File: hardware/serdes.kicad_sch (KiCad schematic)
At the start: 21 parts, among them U4 GateMate-CCGM1A1, X2 511FCA100M000BAG

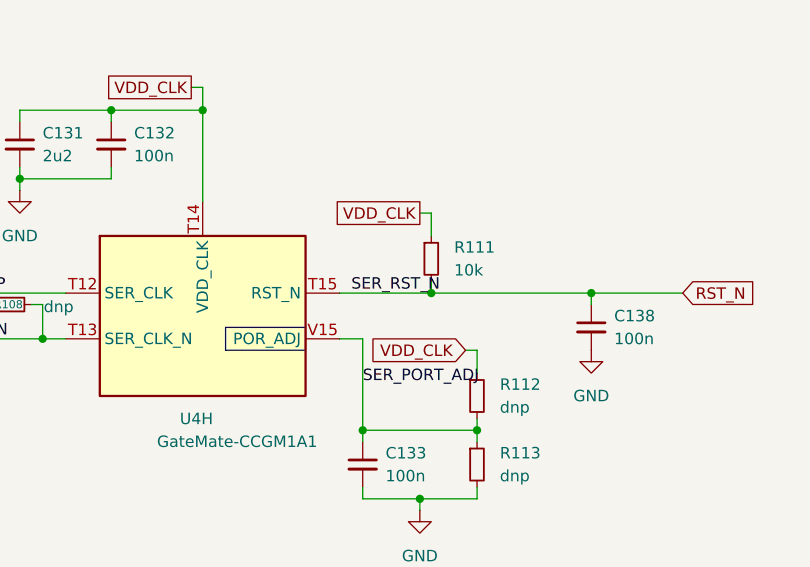
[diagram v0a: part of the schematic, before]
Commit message: power: removed rc filters from gpio domains
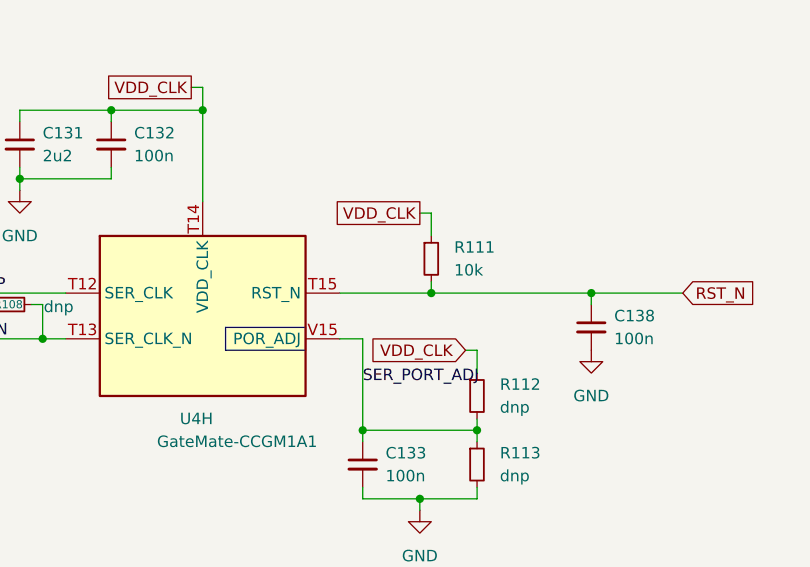
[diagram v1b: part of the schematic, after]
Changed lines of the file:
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@@
-		)
-	)
-	(label "SER_RST_N"
-		(at 125.73 86.36 0)
-		(effects
-			(font
-				(size 1.27 1.27)
-			)
-			(justify left bottom)
 		)
 	)

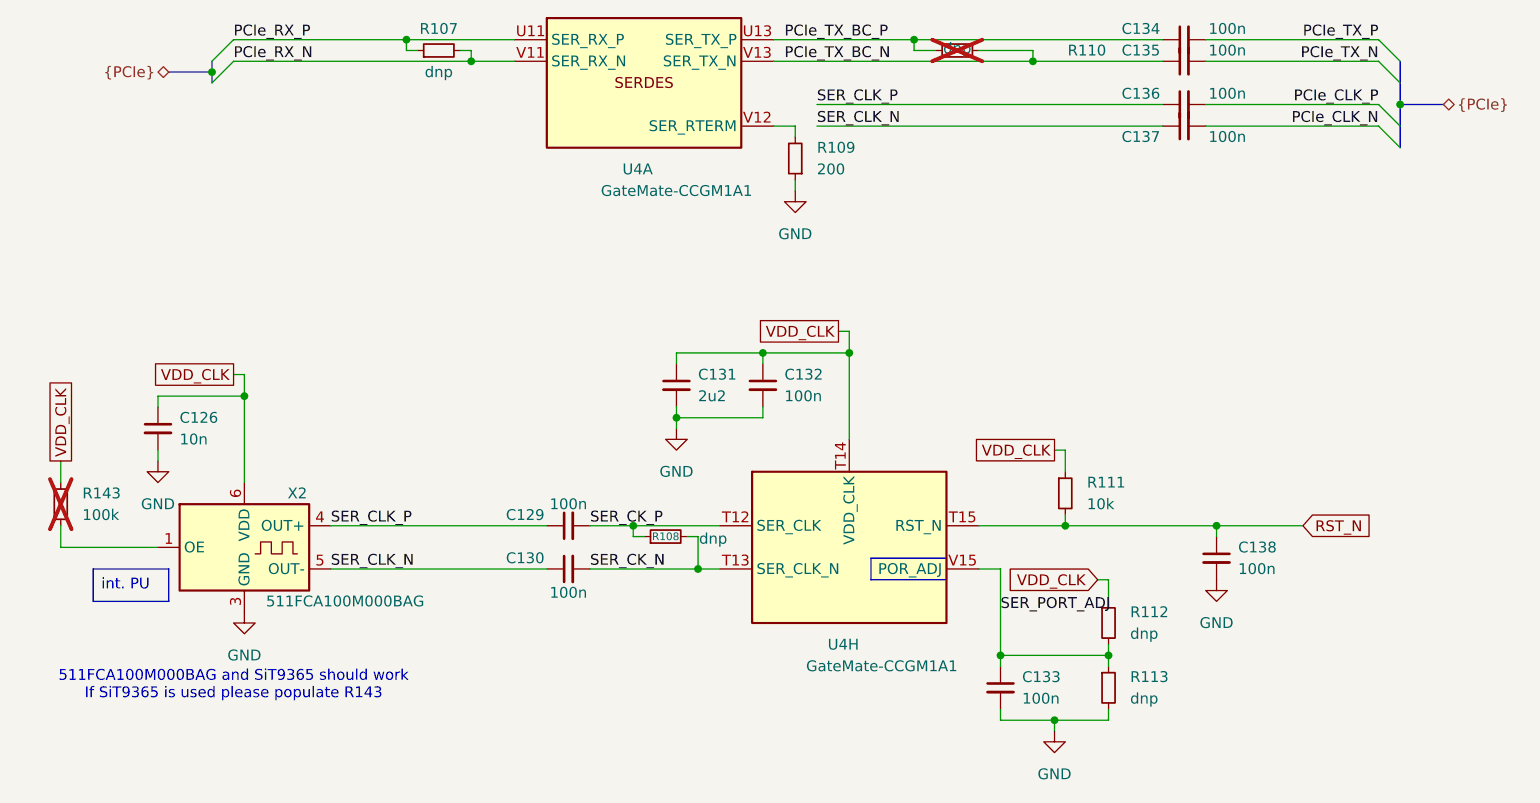
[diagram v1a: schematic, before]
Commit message: serdes: use +1V8 instead of `VDD_CLK`
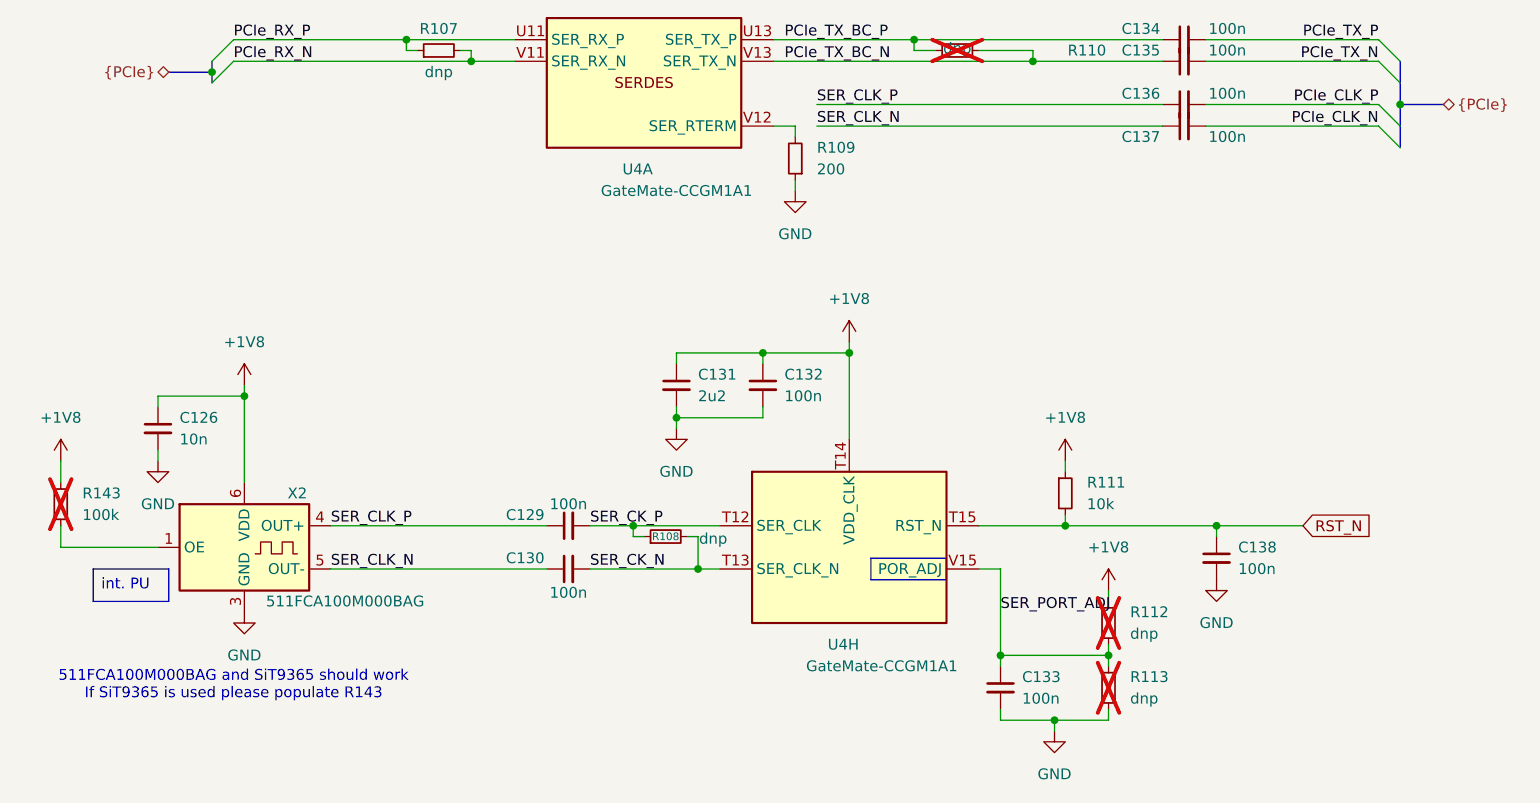
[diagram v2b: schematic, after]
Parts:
- R112, R113: now not fitted
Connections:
- net VDD_CLK renamed +1V8
